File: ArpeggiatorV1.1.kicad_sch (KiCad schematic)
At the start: 67 parts, among them J1 DIN-5_MIDI_IN, J2 DIN-5_SYNC_IN, J3 DIN-5_MIDI_OUT, J4 Conn_01x03_Pin, SW1 SW_SYNC, SW2 SW_MODE, SW3 SW_OCT, SW4 SW_ONOFF, SW5 SW_HOLD, U1 6N138, U2 6N138, U3 Pico

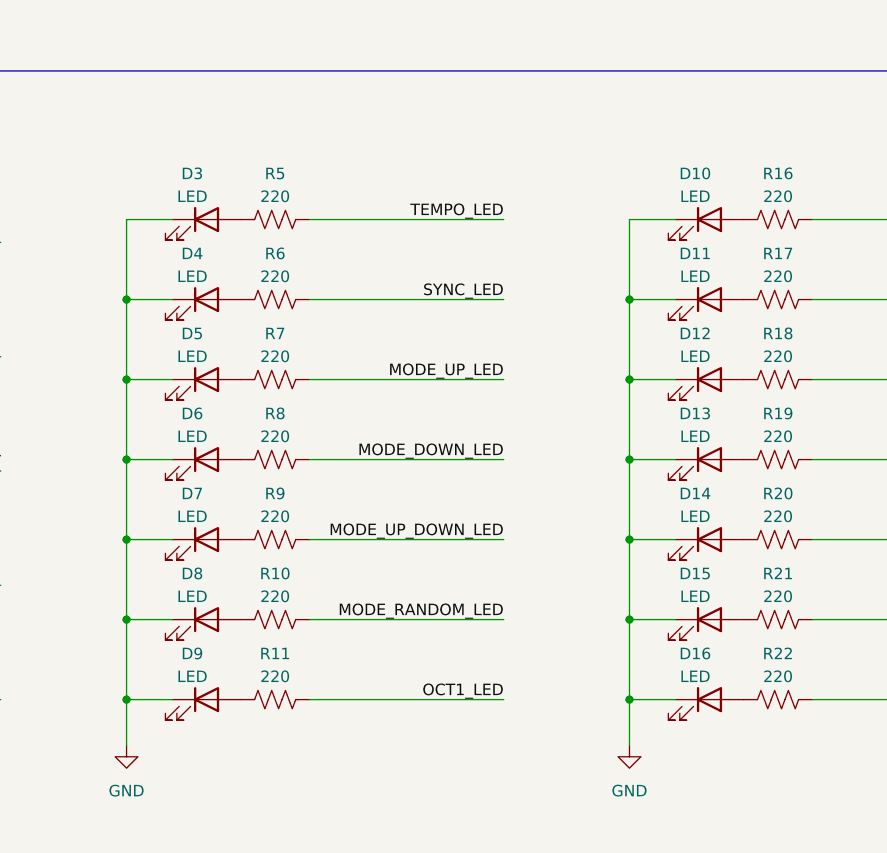
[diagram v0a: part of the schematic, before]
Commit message: Added component values to PCB silkscreen.
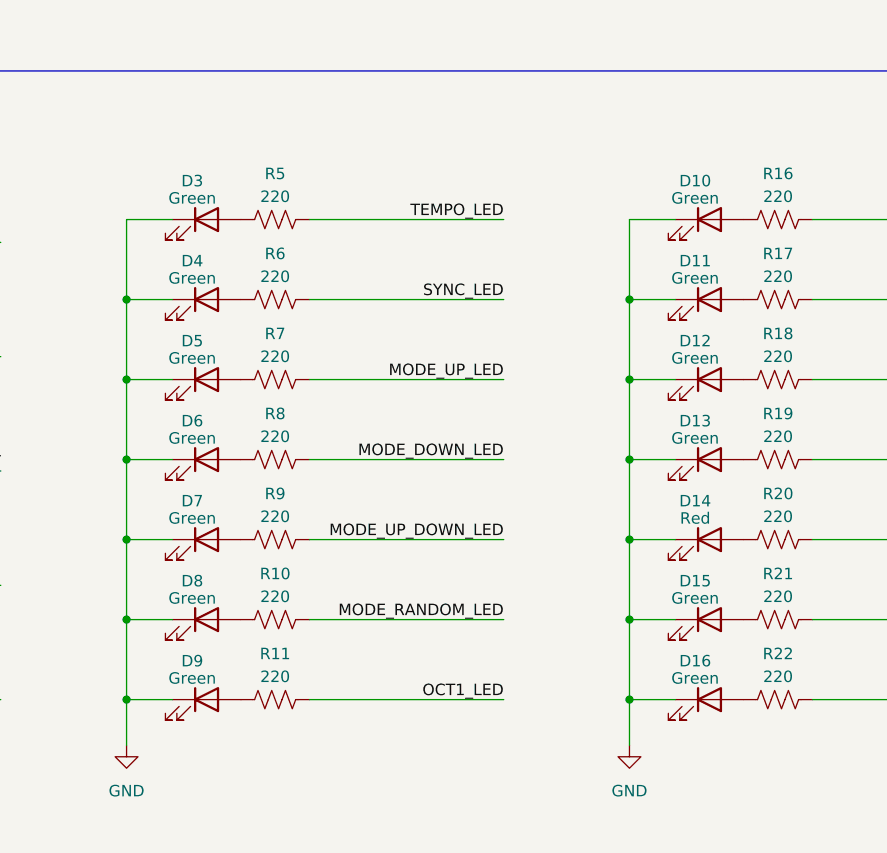
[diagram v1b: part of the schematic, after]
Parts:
- D10, D11, D12, D13, D15, D16, D3, D4, D5, D6, D7, D8, D9: value LED -> Green
- D14: value LED -> Red
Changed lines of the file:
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@@
   (symbol (lib_id "Device:LED") (at 148.59 213.36 0) (unit 1)
     (in_bom yes) (on_board yes) (dnp no) (fields_autoplaced)
-    (property "Reference" "D16" (at 147.0025 208.28 0)
-      (effects (font (size 1.27 1.27)))
-    )
-    (property "Value" "LED" (at 147.0025 210.82 0)
+    (property "Reference" "D16" (at 147.0025 209.0801 0)
+      (effects (font (size 1.27 1.27)))
+    )
+    (property "Value" "Green" (at 147.0025 211.0011 0)
       (effects (font (size 1.27 1.27)))
     )
@@
   (symbol (lib_id "Device:LED") (at 148.59 186.69 0) (unit 1)
     (in_bom yes) (on_board yes) (dnp no) (fields_autoplaced)
-    (property "Reference" "D13" (at 147.0025 181.61 0)
-      (effects (font (size 1.27 1.27)))
-    )
-    (property "Value" "LED" (at 147.0025 184.15 0)
+    (property "Reference" "D13" (at 147.0025 182.4101 0)
+      (effects (font (size 1.27 1.27)))
+    )
+    (property "Value" "Green" (at 147.0025 184.3311 0)
       (effects (font (size 1.27 1.27)))
     )
@@
   (symbol (lib_id "Device:LED") (at 92.71 195.58 0) (unit 1)
     (in_bom yes) (on_board yes) (dnp no) (fields_autoplaced)
-    (property "Reference" "D7" (at 91.1225 190.5 0)
-      (effects (font (size 1.27 1.27)))
-    )
-    (property "Value" "LED" (at 91.1225 193.04 0)
+    (property "Reference" "D7" (at 91.1225 191.3001 0)
+      (effects (font (size 1.27 1.27)))
+    )
+    (property "Value" "Green" (at 91.1225 193.2211 0)
       (effects (font (size 1.27 1.27)))
     )
@@
   (symbol (lib_id "Device:LED") (at 92.71 160.02 0) (unit 1)
     (in_bom yes) (on_board yes) (dnp no) (fields_autoplaced)
-    (property "Reference" "D3" (at 91.1225 154.94 0)
-      (effects (font (size 1.27 1.27)))
-    )
-    (property "Value" "LED" (at 91.1225 157.48 0)
+    (property "Reference" "D3" (at 91.1225 155.7401 0)
+      (effects (font (size 1.27 1.27)))
+    )
+    (property "Value" "Green" (at 91.1225 157.6611 0)
       (effects (font (size 1.27 1.27)))
     )
@@
   (symbol (lib_id "Device:LED") (at 148.59 204.47 0) (unit 1)
     (in_bom yes) (on_board yes) (dnp no) (fields_autoplaced)
-    (property "Reference" "D15" (at 147.0025 199.39 0)
-      (effects (font (size 1.27 1.27)))
-    )
-    (property "Value" "LED" (at 147.0025 201.93 0)
+    (property "Reference" "D15" (at 147.0025 200.1901 0)
+      (effects (font (size 1.27 1.27)))
+    )
+    (property "Value" "Green" (at 147.0025 202.1111 0)
       (effects (font (size 1.27 1.27)))
     )
@@
   (symbol (lib_id "Device:LED") (at 148.59 177.8 0) (unit 1)
     (in_bom yes) (on_board yes) (dnp no) (fields_autoplaced)
-    (property "Reference" "D12" (at 147.0025 172.72 0)
-      (effects (font (size 1.27 1.27)))
-    )
-    (property "Value" "LED" (at 147.0025 175.26 0)
+    (property "Reference" "D12" (at 147.0025 173.5201 0)
+      (effects (font (size 1.27 1.27)))
+    )
+    (property "Value" "Green" (at 147.0025 175.4411 0)
       (effects (font (size 1.27 1.27)))
     )
@@
   (symbol (lib_id "Device:LED") (at 148.59 168.91 0) (unit 1)
     (in_bom yes) (on_board yes) (dnp no) (fields_autoplaced)
-    (property "Reference" "D11" (at 147.0025 163.83 0)
-      (effects (font (size 1.27 1.27)))
-    )
-    (property "Value" "LED" (at 147.0025 166.37 0)
+    (property "Reference" "D11" (at 147.0025 164.6301 0)
+      (effects (font (size 1.27 1.27)))
+    )
+    (property "Value" "Green" (at 147.0025 166.5511 0)
       (effects (font (size 1.27 1.27)))
     )
@@
   (symbol (lib_id "Device:LED") (at 92.71 213.36 0) (unit 1)
     (in_bom yes) (on_board yes) (dnp no) (fields_autoplaced)
-    (property "Reference" "D9" (at 91.1225 208.28 0)
-      (effects (font (size 1.27 1.27)))
-    )
-    (property "Value" "LED" (at 91.1225 210.82 0)
+    (property "Reference" "D9" (at 91.1225 209.0801 0)
+      (effects (font (size 1.27 1.27)))
+    )
+    (property "Value" "Green" (at 91.1225 211.0011 0)
       (effects (font (size 1.27 1.27)))
     )
@@
   (symbol (lib_id "Device:LED") (at 92.71 186.69 0) (unit 1)
     (in_bom yes) (on_board yes) (dnp no) (fields_autoplaced)
-    (property "Reference" "D6" (at 91.1225 181.61 0)
-      (effects (font (size 1.27 1.27)))
-    )
-    (property "Value" "LED" (at 91.1225 184.15 0)
+    (property "Reference" "D6" (at 91.1225 182.4101 0)
+      (effects (font (size 1.27 1.27)))
+    )
+    (property "Value" "Green" (at 91.1225 184.3311 0)
       (effects (font (size 1.27 1.27)))
     )
@@
   (symbol (lib_id "Device:LED") (at 148.59 160.02 0) (unit 1)
     (in_bom yes) (on_board yes) (dnp no) (fields_autoplaced)
-    (property "Reference" "D10" (at 147.0025 154.94 0)
-      (effects (font (size 1.27 1.27)))
-    )
-    (property "Value" "LED" (at 147.0025 157.48 0)
+    (property "Reference" "D10" (at 147.0025 155.7401 0)
+      (effects (font (size 1.27 1.27)))
+    )
+    (property "Value" "Green" (at 147.0025 157.6611 0)
       (effects (font (size 1.27 1.27)))
     )
@@
   (symbol (lib_id "Device:LED") (at 92.71 177.8 0) (unit 1)
     (in_bom yes) (on_board yes) (dnp no) (fields_autoplaced)
-    (property "Reference" "D5" (at 91.1225 172.72 0)
-      (effects (font (size 1.27 1.27)))
-    )
-    (property "Value" "LED" (at 91.1225 175.26 0)
+    (property "Reference" "D5" (at 91.1225 173.5201 0)
+      (effects (font (size 1.27 1.27)))
+    )
+    (property "Value" "Green" (at 91.1225 175.4411 0)
       (effects (font (size 1.27 1.27)))
     )
@@
   (symbol (lib_id "Device:LED") (at 148.59 195.58 0) (unit 1)
     (in_bom yes) (on_board yes) (dnp no) (fields_autoplaced)
-    (property "Reference" "D14" (at 147.0025 190.5 0)
-      (effects (font (size 1.27 1.27)))
-    )
-    (property "Value" "LED" (at 147.0025 193.04 0)
+    (property "Reference" "D14" (at 147.0025 191.3001 0)
+      (effects (font (size 1.27 1.27)))
+    )
+    (property "Value" "Red" (at 147.0025 193.2211 0)
       (effects (font (size 1.27 1.27)))
     )
@@
   (symbol (lib_id "Device:LED") (at 92.71 204.47 0) (unit 1)
     (in_bom yes) (on_board yes) (dnp no) (fields_autoplaced)
-    (property "Reference" "D8" (at 91.1225 199.39 0)
-      (effects (font (size 1.27 1.27)))
-    )
-    (property "Value" "LED" (at 91.1225 201.93 0)
+    (property "Reference" "D8" (at 91.1225 200.1901 0)
+      (effects (font (size 1.27 1.27)))
+    )
+    (property "Value" "Green" (at 91.1225 202.1111 0)
       (effects (font (size 1.27 1.27)))
     )
@@
   (symbol (lib_id "Device:LED") (at 92.71 168.91 0) (unit 1)
     (in_bom yes) (on_board yes) (dnp no) (fields_autoplaced)
-    (property "Reference" "D4" (at 91.1225 163.83 0)
-      (effects (font (size 1.27 1.27)))
-    )
-    (property "Value" "LED" (at 91.1225 166.37 0)
-      (effects (font (size 1.27 1.27)))
-    )
+    (property "Reference" "D4" (at 91.1225 164.6301 0)
+      (effects (font (size 1.27 1.27)))
+    )
+    (property "Value" "Green" (at 91.1225 166.5511 0)
+      (effects (font (size 1.27 1.27)))
+    )

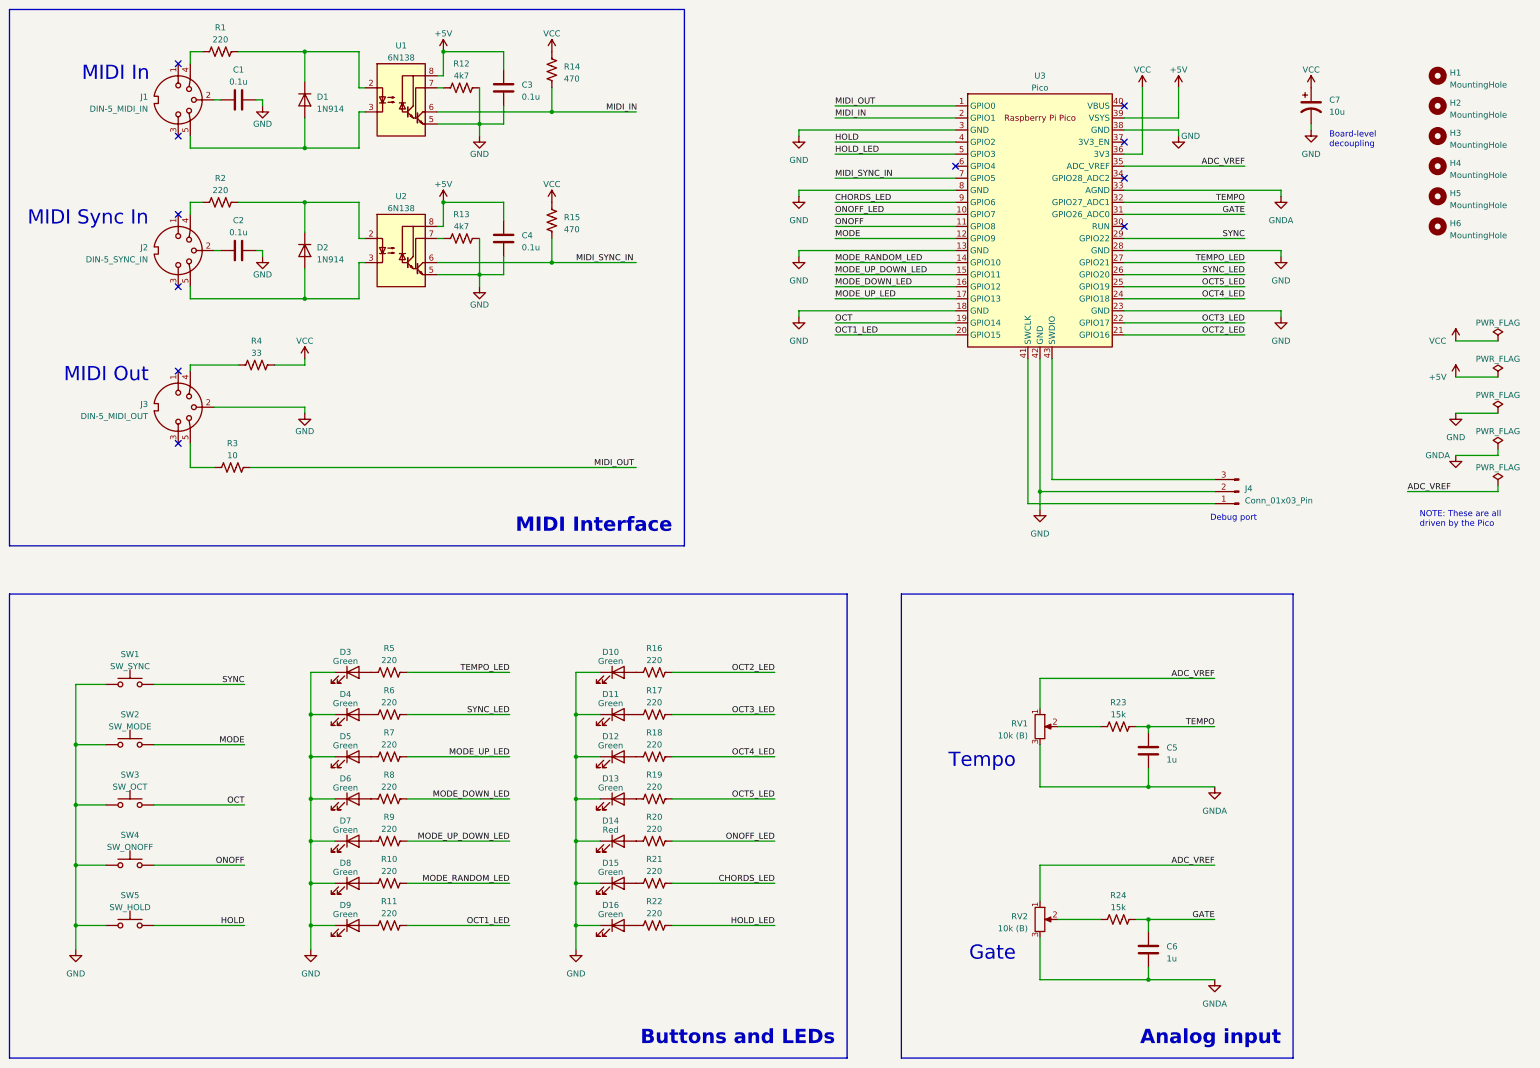
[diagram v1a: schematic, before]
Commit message: Updated schematic+PCB with new MIDI interface section.
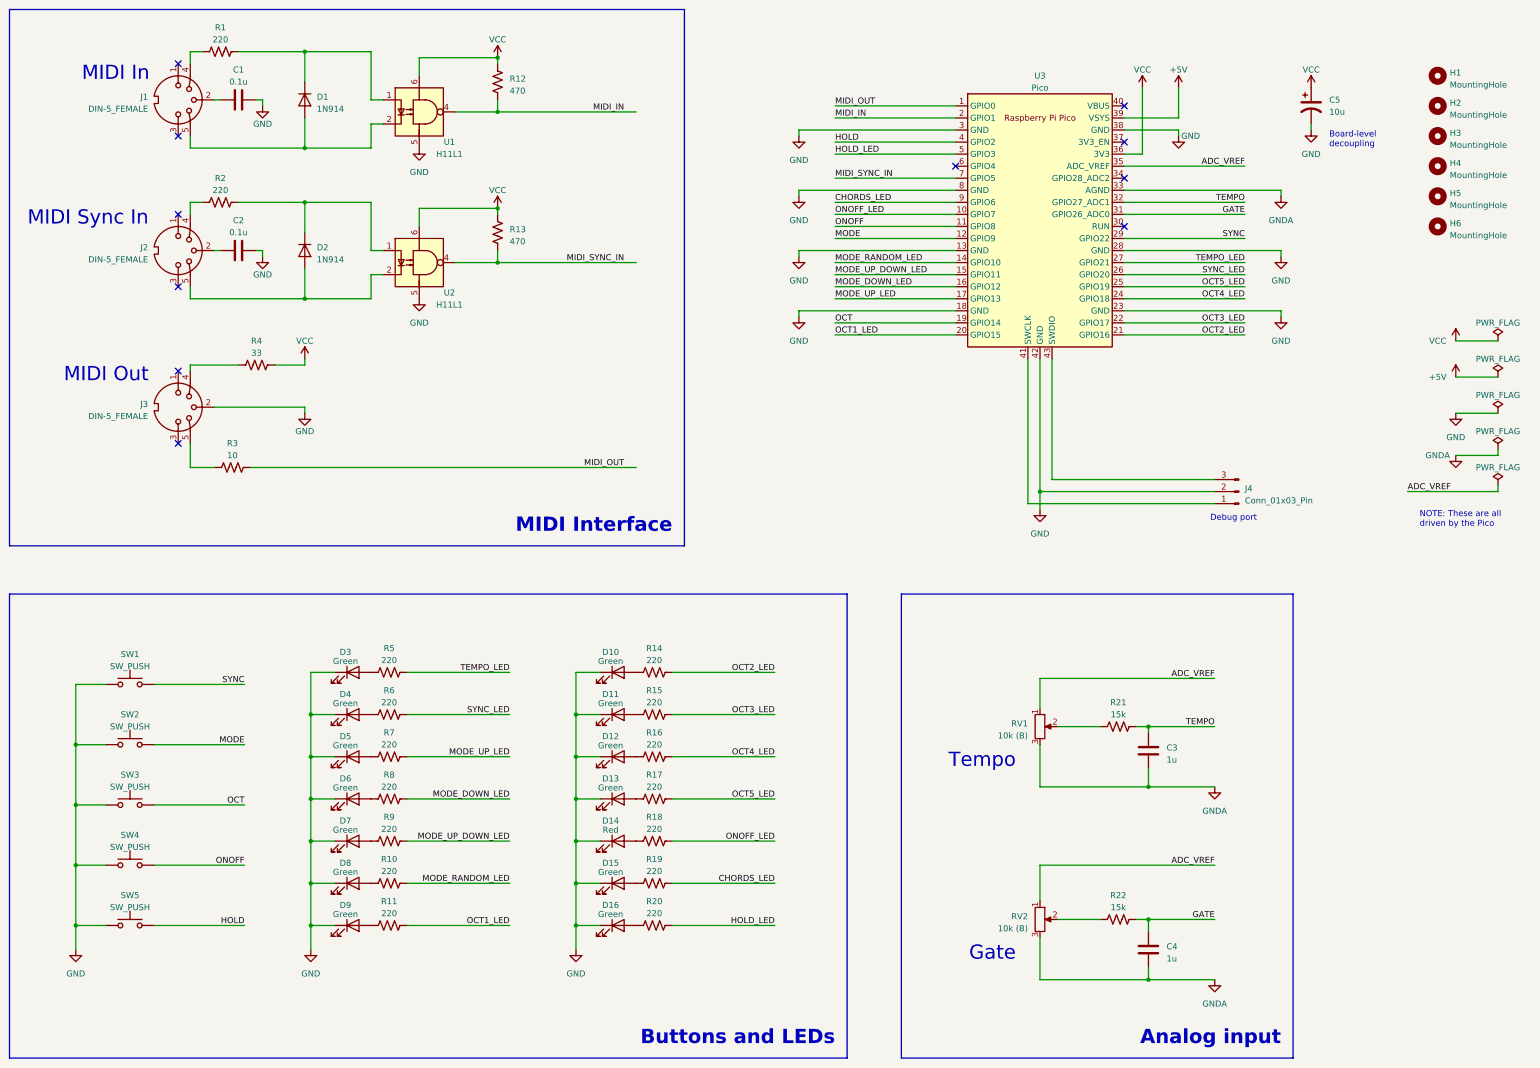
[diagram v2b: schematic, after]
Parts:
- removed C3, C4: 0.1u, Capacitor_THT:C_Disc_D3.0mm_W1.6mm_P2.50mm, symbol Device:C
- removed R14, R15: 470, Resistor_THT:R_Axial_DIN0207_L6.3mm_D2.5mm_P10.16mm_Horizontal, symbol Device:R_US
- removed U1, U2: 6N138, Package_DIP:DIP-8_W7.62mm_LongPads, symbol Isolator:6N138
- added U1, U2: H11L1, Package_DIP:DIP-6_W7.62mm_LongPads, symbol Isolator:H11L1
- J1: value DIN-5_MIDI_IN -> DIN-5_FEMALE
- J2: value DIN-5_SYNC_IN -> DIN-5_FEMALE
- J3: value DIN-5_MIDI_OUT -> DIN-5_FEMALE
- R12, R13: value 4k7 -> 470
- SW1: value SW_SYNC -> SW_PUSH
- SW2: value SW_MODE -> SW_PUSH
- SW3: value SW_OCT -> SW_PUSH
- SW4: value SW_ONOFF -> SW_PUSH
- SW5: value SW_HOLD -> SW_PUSH
- renumbered C5 to C3, C6 to C4, C7 to C5, R16 to R14, R17 to R15, R18 to R16, R19 to R17, R20 to R18, R21 to R19, R22 to R20, R23 to R21, R24 to R22
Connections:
- net GND: now also U1.5, U2.5; no longer R12.2, R13.2
- net MIDI_IN: now also R12.2, U1.4
- net MIDI_SYNC_IN: now also R13.2, U2.4
- net VCC: now also R12.1, R13.1, U1.6, U2.6
- net at D1.1 (K), R1.2: now also U1.1
- net at D1.2 (A), J1.5: now also U1.2
- net at D2.1 (K), R2.2: now also U2.1
- net at D2.2 (A), J2.5: now also U2.2
